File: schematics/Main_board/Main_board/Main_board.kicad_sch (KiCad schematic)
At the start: 7 parts, among them J1 USB_B_Micro, J2 Conn_01x16_Female, U1 ESP32-S3-WROOM-1, U2 AP2112K-3.3, U3 AP9101CK6, U4 CH340G, U5 PCF8563T

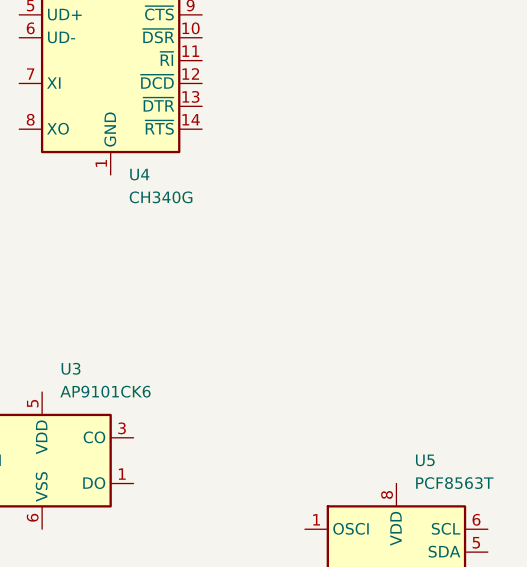
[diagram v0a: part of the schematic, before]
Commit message: Update: Added LCD symbol
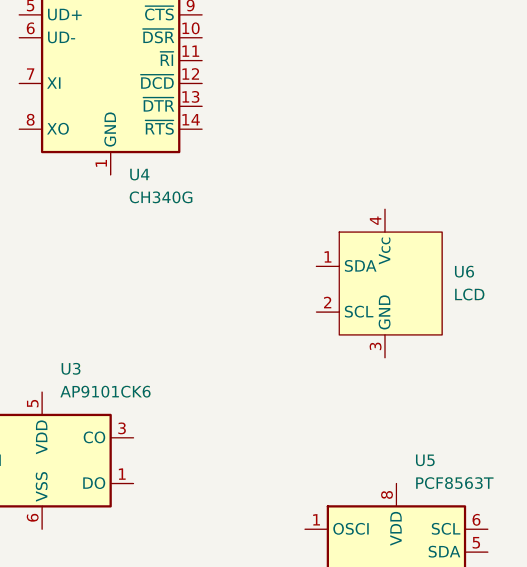
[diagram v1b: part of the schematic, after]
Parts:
- added U6: LCD, LCD:LCD_IIC_12864, symbol LCD_IIC_12864:LCD
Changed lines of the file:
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@@
 (kicad_sch (version 20211123) (generator eeschema)
   (paper "A4")
+  (symbol (lib_id "LCD_IIC_12864:LCD") (at 233.68 93.98 0) (unit 1)
+    (in_bom yes) (on_board yes) (fields_autoplaced)
+    (property "Reference" "U6" (id 0) (at 242.57 92.0749 0)
+      (effects (font (size 1.27 1.27)) (justify left))
+    )
+    (property "Value" "LCD" (id 1) (at 242.57 94.6149 0)
+      (effects (font (size 1.27 1.27)) (justify left))
+    )
+    (property "Footprint" "LCD:LCD_IIC_12864" (id 2) (at 233.68 93.98 0)
+      (effects (font (size 1.27 1.27)) hide)
+    )
+    (property "Datasheet" "" (id 3) (at 233.68 93.98 0)
+      (effects (font (size 1.27 1.27)) hide)
+    )
+    (pin "1")
+    (pin "2")
+    (pin "3")
+    (pin "4")
+  )
   (symbol (lib_id "Connector:Conn_01x16_Female") (at 127 161.29 0) (unit 1)
     (in_bom yes) (on_board yes) (fields_autoplaced)
@@
       (reference "U5") (unit 1) (value "PCF8563T") (footprint "Package_SO:SOIC-8_3.9x4.9mm_P1.27mm")
     )
-  )
+    (path "/273e77b9-cb3a-4fba-ac11-4ce2cd073300"
+      (reference "U6") (unit 1) (value "LCD") (footprint "LCD:LCD_IIC_12864")
+    )
+  )

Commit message: Update: added new schematics components
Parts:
- added BT1: 1v5 LR44, LCD:MY-LR44-02, symbol Device:Battery_Cell
- added BT2: 3v7 LIpo, symbol Device:Battery_Cell
- added C1, C2, C3: 1uf, Capacitor_SMD:C_0201_0603Metric, symbol Device:C
- added C4, C5: 33p, Capacitor_SMD:C_0201_0603Metric, symbol Device:C
- added C6, C7: 0.1u, Capacitor_SMD:C_0201_0603Metric, symbol Device:C
- added U?: LSM6DS3, Package_LGA:LGA-14_3x2.5mm_P0.5mm_LayoutBorder3x4y, symbol Sensor_Motion:LSM6DS3
- added Y1: 12Mhz, Crystal:Resonator_SMD_Murata_CSTxExxV-3Pin_3.0x1.1mm_HandSoldering, symbol Device:Crystal
- added Y2: 32.768kHz, Crystal:Crystal_C38-LF_D3.0mm_L8.0mm_Horizontal, symbol Device:Crystal
- U3: value AP9101CK6 -> BQ21040DBVR
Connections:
- net SDA_1: now reaches U6.1 (SDA)
- net SCL_1: now reaches U6.2 (SCL)
- net GNDREF: now reaches U6.3 (GND)
- net GNDREF: now also J1.4 (ID), J1.5 (GND), J1.6 (Shield), J2.15 (Pin_15), J2.16 (Pin_16), U2.2 (GND), U3.6 (VSS), U4.1 (GND), C1.2, C2.2, C3.2, C4.2, C5.2, C6.1, C7.2
- net +3V3: now reaches U6.4 (Vcc)
- net +3V3: now also J2.1 (Pin_1), J2.2 (Pin_2), U2.5 (VOUT), C2.1
- net I/O_1: now reaches J2.10 (Pin_10)
- net I/O_2: now reaches J2.11 (Pin_11)
- net I/O_3: now reaches J2.12 (Pin_12)
- net I/O_4: now reaches J2.13 (Pin_13)
- net I/O_5: now reaches J2.14 (Pin_14)
- net UART_TX: now reaches J2.3 (Pin_3)
- net UART_RX: now reaches J2.4 (Pin_4)
- net MOSI: now reaches J2.5 (Pin_5)
- net MISO: now reaches J2.6 (Pin_6)
- net CLK: now reaches J2.7 (Pin_7)
- net SDA_2: now reaches J2.8 (Pin_8)
- net SCL_2: now reaches J2.9 (Pin_9)
- net +5V: now reaches U4.16 (VCC)
- net +5V: now also J1.1 (VBUS), C7.1
- net UART_TX0_PGR: now reaches U4.2 (TXD)
- net UART_TX0_PGR: now also U1.36 (U0RXD/GPIO44/CLK_OUT2)
- net UART_RX0_PGR: now reaches U4.3 (RXD)
- net UART_RX0_PGR: now also U1.37 (U0TXD/GPIO43/CLK_OUT1)
- net at U4.4 (V3): now also C6.2
- net D+: now reaches U4.5 (UD+)
- net D+: now also J1.3 (D+)
- net D-: now reaches U4.6 (UD-)
- net D-: now also J1.2 (D-)
- net at U4.7 (XI): now also C5.1, Y1.2
- net at U4.8 (XO): now also C4.1, Y1.1
- net +BATT: now reaches U2.1 (VIN)
- net +BATT: now also U2.3 (EN), C1.1
- net at U3.5 (VDD): now also C3.1
- no-connect marks 0 -> 7
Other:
- note added: "- Add short circuit protection - Make test circuit before conect MCU - Add ESD Protection - Create new extended footprint for LIS3DH"
- note added: "Battery management system"
- note added: "LCD Screen 128x64"
- note added: "MPU"
- note added: "Power Regulator"
- note added: "Real Time clock"
- note added: "To do:"
- note added: "USB Programming Connection"
- moved on the sheet: J1, J2, U2, U4, U5, U6

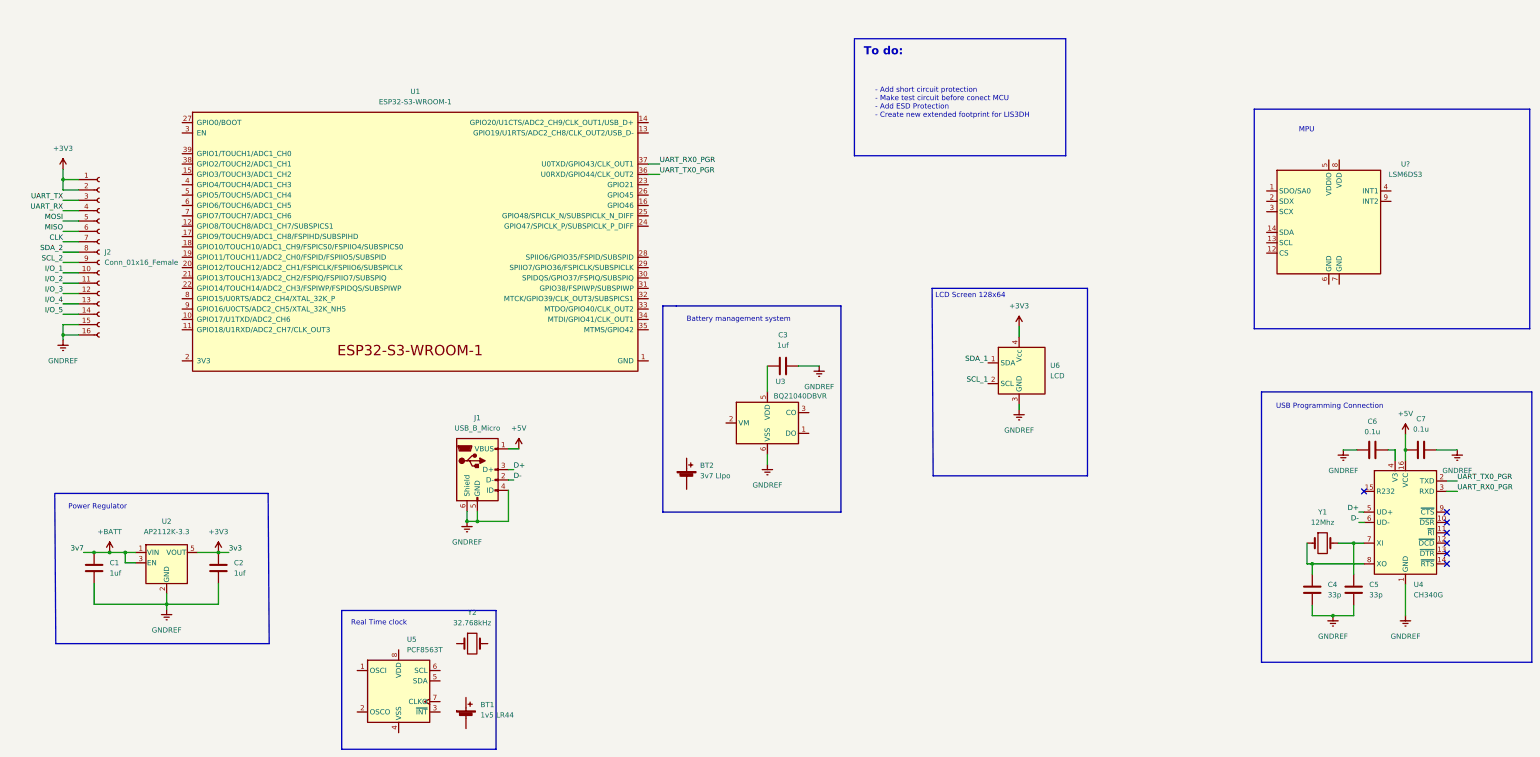
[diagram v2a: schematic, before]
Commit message: Update: add components to schematics
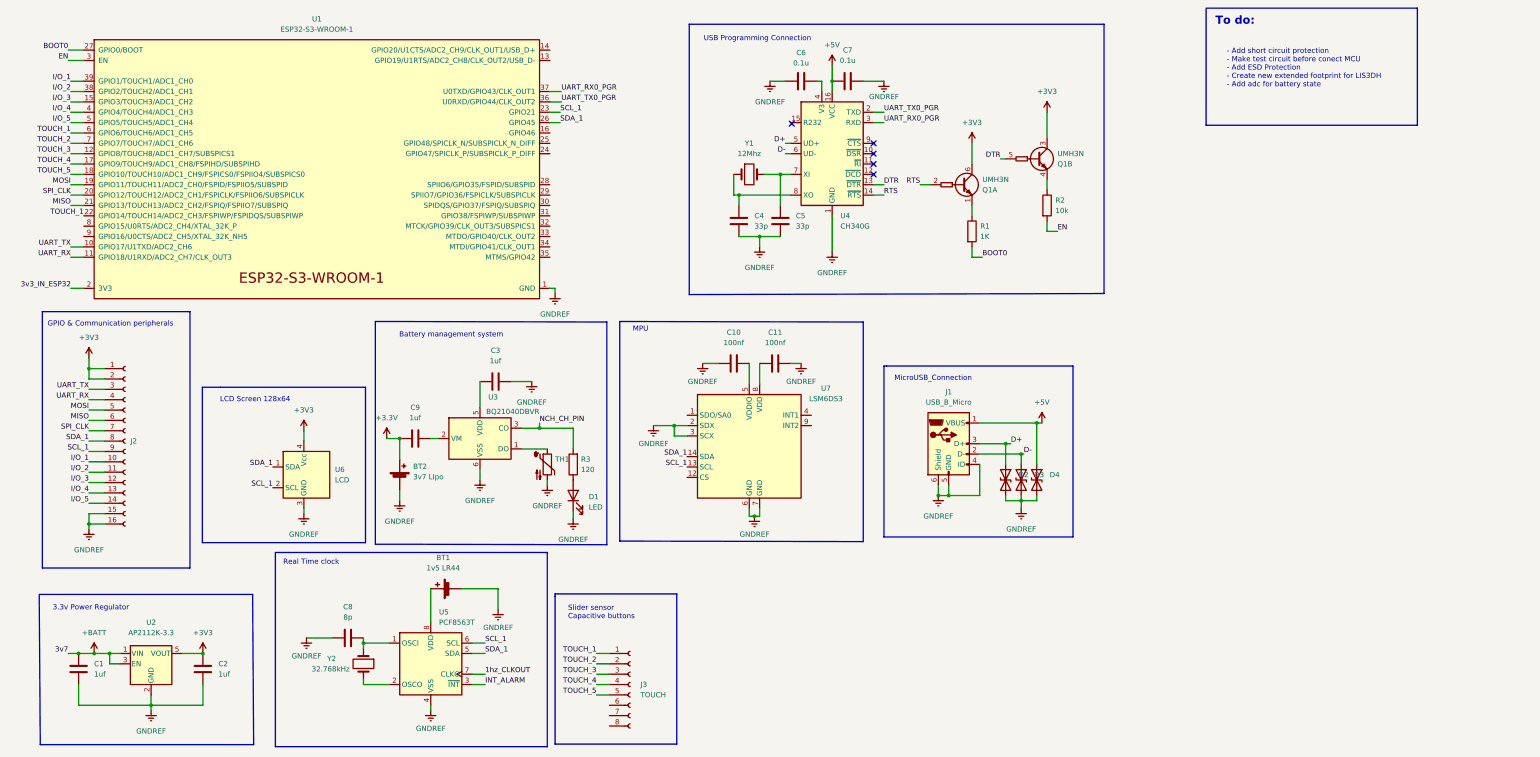
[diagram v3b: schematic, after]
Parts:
- added C10, C11: 100nf, Capacitor_SMD:C_0201_0603Metric, symbol Device:C
- added C8: 8p, Capacitor_SMD:C_0201_0603Metric, symbol Device:C
- added C9: 1uf, Capacitor_SMD:C_0201_0603Metric, symbol Device:C
- added D1: LED, LED_SMD:LED_0402_1005Metric_Pad0.77x0.64mm_HandSolder, symbol Device:LED
- added D2, D3: TPD1E10B06DPYR, symbol Device:D_TVS
- added D4: TPD1E10B06DPYR, Resistor_SMD:R_0603_1608Metric, symbol Device:D_TVS
- added J3: TOUCH, LCD:slide_sensor_8p, symbol Connector:Conn_01x08_Female
- added Q1: UMH3N, Package_TO_SOT_SMD:SOT-363_SC-70-6, symbol Transistor_BJT:UMH3N
- added R1: 1K, Resistor_SMD:R_0201_0603Metric_Pad0.64x0.40mm_HandSolder, symbol Device:R
- added R2: 10k, Resistor_SMD:R_0201_0603Metric_Pad0.64x0.40mm_HandSolder, symbol Device:R
- added R3: 120, Resistor_SMD:R_0201_0603Metric_Pad0.64x0.40mm_HandSolder, symbol Device:R
- added TH1: NCP18XH103F03RB, Resistor_SMD:R_0603_1608Metric, symbol Device:Thermistor_NTC
- gave numbers to parts that had none: 1
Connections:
- net CLK is gone; now on net SPI_CLK: J2.7 (Pin_7)
- net SCL_2 is gone; now on net SCL_1: J2.9 (Pin_9)
- net SDA_2 is gone; now on net SDA_1: J2.8 (Pin_8)
- net +3V3: now also Q1.3 (C2), Q1.6 (C1)
- net +5V: now also D4.1 (A1)
- net D+: now also D2.1 (A1)
- net D-: now also D3.1 (A1)
- net GNDREF: now also BT1.2 (-), BT2.2 (-), U1.1 (GND), U1.40 (GND), U1.41 (GND), U5.4 (VSS), U7.2 (SDX), U7.3 (SCX), U7.6 (GND), U7.7 (GND), C10.2, C11.1, C8.2, D1.1 (K), D2.2 (A2), D3.2 (A2), D4.2 (A2), TH1.2
- net I/O_1: now also U1.39 (GPIO1/TOUCH1/ADC1_CH0)
- net I/O_2: now also U1.38 (GPIO2/TOUCH2/ADC1_CH1)
- net I/O_3: now also U1.15 (GPIO3/TOUCH3/ADC1_CH2)
- net I/O_4: now also U1.4 (GPIO4/TOUCH4/ADC1_CH3)
- net I/O_5: now also U1.5 (GPIO5/TOUCH5/ADC1_CH4)
- net MISO: now also U1.21 (GPIO13/TOUCH13/ADC2_CH2/FSPIQ/FSPIIO7/SUBSPIQ)
- net MOSI: now also U1.19 (GPIO11/TOUCH11/ADC2_CH0/FSPID/FSPIIO5/SUBSPID)
- net SCL_1: now also U1.23 (GPIO21), U5.6 (SCL), U7.13 (SCL)
- net SDA_1: now also U1.26 (GPIO45), U5.5 (SDA), U7.14 (SDA)
- net UART_RX: now also U1.11 (GPIO18/U1RXD/ADC2_CH7/CLK_OUT3)
- net UART_TX: now also U1.10 (GPIO17/U1TXD/ADC2_CH6)
- net DTR: now reaches U4.13 (~{DTR})
- net DTR: now also Q1.5 (B2)
- net RTS: now reaches U4.14 (~{RTS})
- net RTS: now also Q1.2 (B1)
- net at BT1.1 (+): now also U5.8 (VDD)
- net TOUCH_3: now reaches U1.12 (GPIO8/TOUCH8/ADC1_CH7/SUBSPICS1)
- net TOUCH_3: now also J3.3 (Pin_3)
- net TOUCH_4: now reaches U1.17 (GPIO9/TOUCH9/ADC1_CH8/FSPIHD/SUBSPIHD)
- net TOUCH_4: now also J3.4 (Pin_4)
- net TOUCH_5: now reaches U1.18 (GPIO10/TOUCH10/ADC1_CH9/FSPICS0/FSPIIO4/SUBSPICS0)
- net TOUCH_5: now also J3.5 (Pin_5)
- net 3v3_IN_ESP32: now reaches U1.2 (3V3)
- net SPI_CLK: now reaches U1.20 (GPIO12/TOUCH12/ADC2_CH1/FSPICLK/FSPIIO6/SUBSPICLK)
- net TOUCH_1: now reaches U1.22 (GPIO14/TOUCH14/ADC2_CH3/FSPIWP/FSPIDQS/SUBSPIWP)
- net TOUCH_1: now also U1.6 (GPIO6/TOUCH6/ADC1_CH5), J3.1 (Pin_1)
- net BOOT0: now reaches U1.27 (GPIO0/BOOT)
- net BOOT0: now also R1.2
- net EN: now reaches U1.3 (EN)
- net EN: now also R2.2
- net TOUCH_2: now reaches U1.7 (GPIO7/TOUCH7/ADC1_CH6)
- net TOUCH_2: now also J3.2 (Pin_2)
- net at U7.5 (VDDIO): now also C10.1
- net at U7.8 (VDD): now also C11.2
- net at Y2.1: now also U5.1 (OSCI), C8.1
- net at Y2.2: now also U5.2 (OSCO)
- net at U3.1 (DO): now also TH1.1
- net at U3.2 (VM): now also C9.2
- net NCH_CH_PIN: now reaches U3.3 (CO)
- net NCH_CH_PIN: now also R3.2
- net INT_ALARM: now reaches U5.3 (~{INT})
- net 1hz_CLKOUT: now reaches U5.7 (CLKO)
- net +3.3V: now reaches BT2.1 (+)
- net +3.3V: now also C9.1
- new net: Q1.1 (E1), R1.1
- new net: Q1.4 (E2), R2.1
- new net: D1.2 (A), R3.1
- no-connect marks 7 -> 5
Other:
- note added: "- Add short circuit protection - Make test circuit before conect MCU - Add ESD Protection - Create new extended footprint for LIS3DH - Add adc for battery state"
- note added: "3.3v Power Regulator"
- note added: "GPIO & Communication peripherals"
- note added: "MicroUSB_Connection"
- note added: "Slider sensor Capacitive buttons"
- note removed: "- Add short circuit protection - Make test circuit before conect MCU - Add ESD Protection - Create new extended footprint for LIS3DH"
- note removed: "Power Regulator"
- moved on the sheet: BT1, BT2, C1, C2, C3, C4, C5, C6, C7, J1, J2, U1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

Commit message: Update: added datasheet to KiCad component
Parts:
- added R4, R5: 4k7, Resistor_SMD:R_0603_1608Metric_Pad0.98x0.95mm_HandSolder, symbol Device:R
- D2, D3: value TPD1E10B06DPYR -> 0603ESDA-05N; footprint (none) -> Resistor_SMD:R_0603_1608Metric
- D4: value TPD1E10B06DPYR -> 0603ESDA-05N
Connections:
- net +3.3V: now also U7.12 (CS)
- net +3V3: now also C10.1, C11.2, U7.5 (VDDIO), U7.8 (VDD), R4.2, R5.1
- net GNDREF: now also U7.1 (SDO/SA0)
- net SCL_1: now also R5.2
- net SDA_1: now also R4.1
- net INT_1_MPU: now reaches U7.4 (INT1)
- net INT_2_MPU: now reaches U7.9 (INT2)
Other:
- note added: "Attitude Sensor/Gyroscope"
- note added: "SDO/SA0 pin is connected to ground, the LSb value is '0' (address 1101010b)"
- note added: "i2c Pull-up resistors"
- note removed: "MPU"
- moved on the sheet: C1, C10, C11, C2, D4, J1, J3, U2, U6, U7

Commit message: Update: added a new field for kicad components for the #lcsc part
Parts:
- C1, C2, C3, C9: #LCSC Part (none) -> C59302
- C10, C11: #LCSC Part (none) -> C14663
- C6, C7, C8, J2, R1: #LCSC Part (none) -> re
- D2, D3, D4: #LCSC Part (none) -> C316054
- J1: #LCSC Part (none) -> C132563
- R4, R5: #LCSC Part (none) -> C25804
- U1: footprint esp:ESP32-S3-WROOM-2 -> esp:ESP32-S3-WROOM-1; #LCSC Part (none) -> C2913203
- U2: #LCSC Part (none) -> C51118
- U3: #LCSC Part (none) -> C202311
- U4: #LCSC Part (none) -> C14267
- U5: #LCSC Part (none) -> C7440
- U7: #LCSC Part (none) -> C967633
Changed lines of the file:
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@@
+      (effects (font (size 1.27 1.27)) hide)
+    )
+    (property "#LCSC Part" "re" (id 4) (at 205.105 29.21 0)
       (effects (font (size 1.27 1.27)) hide)
     )
@@
     )
     (property "Datasheet" "~" (id 3) (at 39.37 117.475 0)
+      (effects (font (size 1.27 1.27)) hide)
+    )
+    (property "#LCSC Part" "re" (id 4) (at 39.37 117.475 0)
       (effects (font (size 1.27 1.27)) hide)
     )
@@
       (effects (font (size 1.27 1.27)) hide)
     )
+    (property "#LCSC Part" "C14267" (id 4) (at 212.725 46.99 0)
+      (effects (font (size 1.27 1.27)) hide)
+    )
     (pin "1")
     (pin "10")
@@
       (effects (font (size 1.27 1.27)) hide)
     )
+    (property "#LCSC Part" "C59302" (id 4) (at 560.07 191.135 0)
+      (effects (font (size 1.27 1.27)) hide)
+    )
     (pin "1")
     (pin "2")
@@
       (effects (font (size 1.27 1.27)) hide)
     )
+    (property "#LCSC Part" "C25804" (id 4) (at 537.845 231.775 0)
+      (effects (font (size 1.27 1.27)) hide)
+    )
     (pin "1")
     (pin "2")
@@
       (effects (font (size 1.27 1.27)) hide)
     )
+    (property "#LCSC Part" "C25804" (id 4) (at 530.86 231.775 0)
+      (effects (font (size 1.27 1.27)) hide)
+    )
     (pin "1")
     (pin "2")
@@
     )
     (property "Datasheet" "https://datasheet.lcsc.com/lcsc/1809192242_Diodes-Incorporated-AP2112K-3-3TRG1_C51118.pdf" (id 3) (at 547.37 187.325 0)
+      (effects (font (size 1.27 1.27)) hide)
+    )
+    (property "#LCSC Part" "C51118" (id 4) (at 547.37 189.865 0)
       (effects (font (size 1.27 1.27)) hide)
     )
@@
       (effects (font (size 1.27 1.27)) hide)
     )
+    (property "#LCSC Part" "C59302" (id 4) (at 110.49 116.84 0)
+      (effects (font (size 1.27 1.27)) hide)
+    )
     (pin "1")
     (pin "2")
@@
       (effects (font (size 1.27 1.27)) hide)
     )
+    (property "#LCSC Part" "re" (id 4) (at 93.98 165.735 0)
+      (effects (font (size 1.27 1.27)) hide)
+    )
     (pin "1")
     (pin "2")
@@
     (property "Reference" "U1" (id 0) (at 86.36 13.97 0))
     (property "Value" "ESP32-S3-WROOM-1" (id 1) (at 86.36 16.51 0))
-    (property "Footprint" "esp:ESP32-S3-WROOM-2" (id 2) (at 85.09 85.09 0)
+    (property "Footprint" "esp:ESP32-S3-WROOM-1" (id 2) (at 85.09 85.09 0)
       (effects (font (size 1.27 1.27)) hide)
     )
     (property "Datasheet" "https://www.espressif.com/sites/default/files/documentation/esp32-s3-wroom-1_wroom-1u_datasheet_en.pdf" (id 3) (at 85.09 87.63 0)
+      (effects (font (size 1.27 1.27)) hide)
+    )
+    (property "#LCSC Part" "C2913203" (id 4) (at 85.09 52.07 0)
       (effects (font (size 1.27 1.27)) hide)
     )
@@
       (effects (font (size 1.27 1.27)) hide)
     )
+    (property "#LCSC Part" "C14663" (id 4) (at 426.085 236.22 0)
+      (effects (font (size 1.27 1.27)) hide)
+    )
     (pin "1")
     (pin "2")
@@
     )
     (property "Datasheet" "https://datasheet.lcsc.com/lcsc/2211101700_YAGEO-CC0603KRX7R9BB104_C14663.pdf" (id 3) (at 436.245 236.22 0)
+      (effects (font (size 1.27 1.27)) hide)
+    )
+    (property "#LCSC Part" "C14663" (id 4) (at 436.245 236.22 0)
       (effects (font (size 1.27 1.27)) hide)
     )
@@
     )
     (property "Datasheet" "https://datasheet.lcsc.com/lcsc/2102261805_STMicroelectronics-LSM6DS3TR-C_C967633.pdf" (id 3) (at 432.435 273.05 0)
+      (effects (font (size 1.27 1.27)) hide)
+    )
+    (property "#LCSC Part" "C967633" (id 4) (at 429.895 256.54 0)
       (effects (font (size 1.27 1.27)) hide)
     )
@@
       (effects (font (size 1.27 1.27)) hide)
     )
+    (property "#LCSC Part" "C59302" (id 4) (at 529.59 191.135 0)
+      (effects (font (size 1.27 1.27)) hide)
+    )
     (pin "1")
     (pin "2")
@@
       (effects (font (size 1.27 1.27)) hide)
     )
+    (property "#LCSC Part" "C59302" (id 4) (at 130.175 102.87 0)
+      (effects (font (size 1.27 1.27)) hide)
+    )
     (pin "1")
     (pin "2")
@@
       (effects (font (size 1.27 1.27)) hide)
     )
+    (property "#LCSC Part" "C316054" (id 4) (at 498.475 242.57 0)
+      (effects (font (size 1.27 1.27)) hide)
+    )
     (pin "1")
     (pin "2")
@@
       (effects (font (size 1.27 1.27)) hide)
     )
+    (property "#LCSC Part" "C316054" (id 4) (at 506.095 242.57 0)
+      (effects (font (size 1.27 1.27)) hide)
+    )
     (pin "1")
     (pin "2")
@@
       (effects (font (size 1.27 1.27)) hide)
     )
+    (property "#LCSC Part" "re" (id 4) (at 216.535 29.21 0)
+      (effects (font (size 1.27 1.27)) hide)
+    )
     (pin "1")
     (pin "2")
@@
     )
     (property "Datasheet" "https://datasheet.lcsc.com/lcsc/1811131822_Amphenol-ICC-10118194-0001LF_C132563.pdf" (id 3) (at 488.315 234.95 0)
+      (effects (font (size 1.27 1.27)) hide)
+    )
+    (property "#LCSC Part" "C132563" (id 4) (at 484.505 233.68 0)
       (effects (font (size 1.27 1.27)) hide)
     )
@@
       (effects (font (size 1.27 1.27)) hide)
     )
+    (property "#LCSC Part" "C316054" (id 4) (at 502.285 242.57 0)
+      (effects (font (size 1.27 1.27)) hide)
+    )
     (pin "1")
     (pin "2")
@@
     )
     (property "Datasheet" "https://datasheet.lcsc.com/lcsc/1810101925_Texas-Instruments-BQ21040DBVR_C202311.pdf" (id 3) (at 126.365 115.57 0)
+      (effects (font (size 1.27 1.27)) hide)
+    )
+    (property "#LCSC Part" "C202311" (id 4) (at 126.365 116.84 0)
       (effects (font (size 1.27 1.27)) hide)
     )
@@
       (effects (font (size 1.27 1.27)) hide)
     )
+    (property "#LCSC Part" "re" (id 4) (at 247.015 66.04 0)
+      (effects (font (size 1.27 1.27)) hide)
+    )
     (pin "1")
     (pin "2")
@@
     )
     (property "Datasheet" "https://datasheet.lcsc.com/lcsc/1809141212_NXP-Semicon-PCF8563T-5-518_C7440.pdf" (id 3) (at 114.3 172.085 0)
+      (effects (font (size 1.27 1.27)) hide)
+    )
+    (property "#LCSC Part" "C7440" (id 4) (at 114.3 172.085 0)
       (effects (font (size 1.27 1.27)) hide)
     )
@@
     )
     (path "/7a0dff3f-250a-4c40-a36c-0c81ad4fc01f"
-      (reference "U1") (unit 1) (value "ESP32-S3-WROOM-1") (footprint "esp:ESP32-S3-WROOM-2")
+      (reference "U1") (unit 1) (value "ESP32-S3-WROOM-1") (footprint "esp:ESP32-S3-WROOM-1")
     )
     (path "/638f1952-d13e-4087-8b79-0d3cdfa50895"
